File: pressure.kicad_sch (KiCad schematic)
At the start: 14 parts, among them U4 TLV9101IDBVR

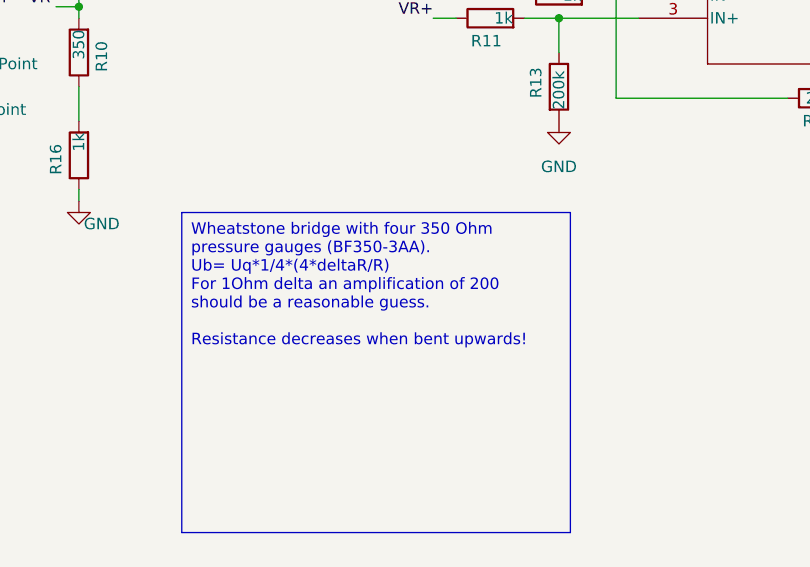
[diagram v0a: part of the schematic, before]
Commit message: update to kicad 9.0 and place Qi-charge IC
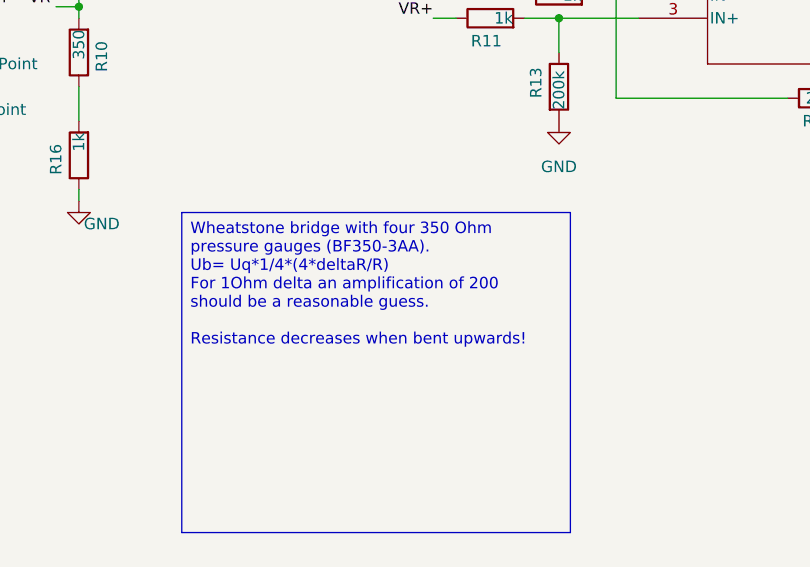
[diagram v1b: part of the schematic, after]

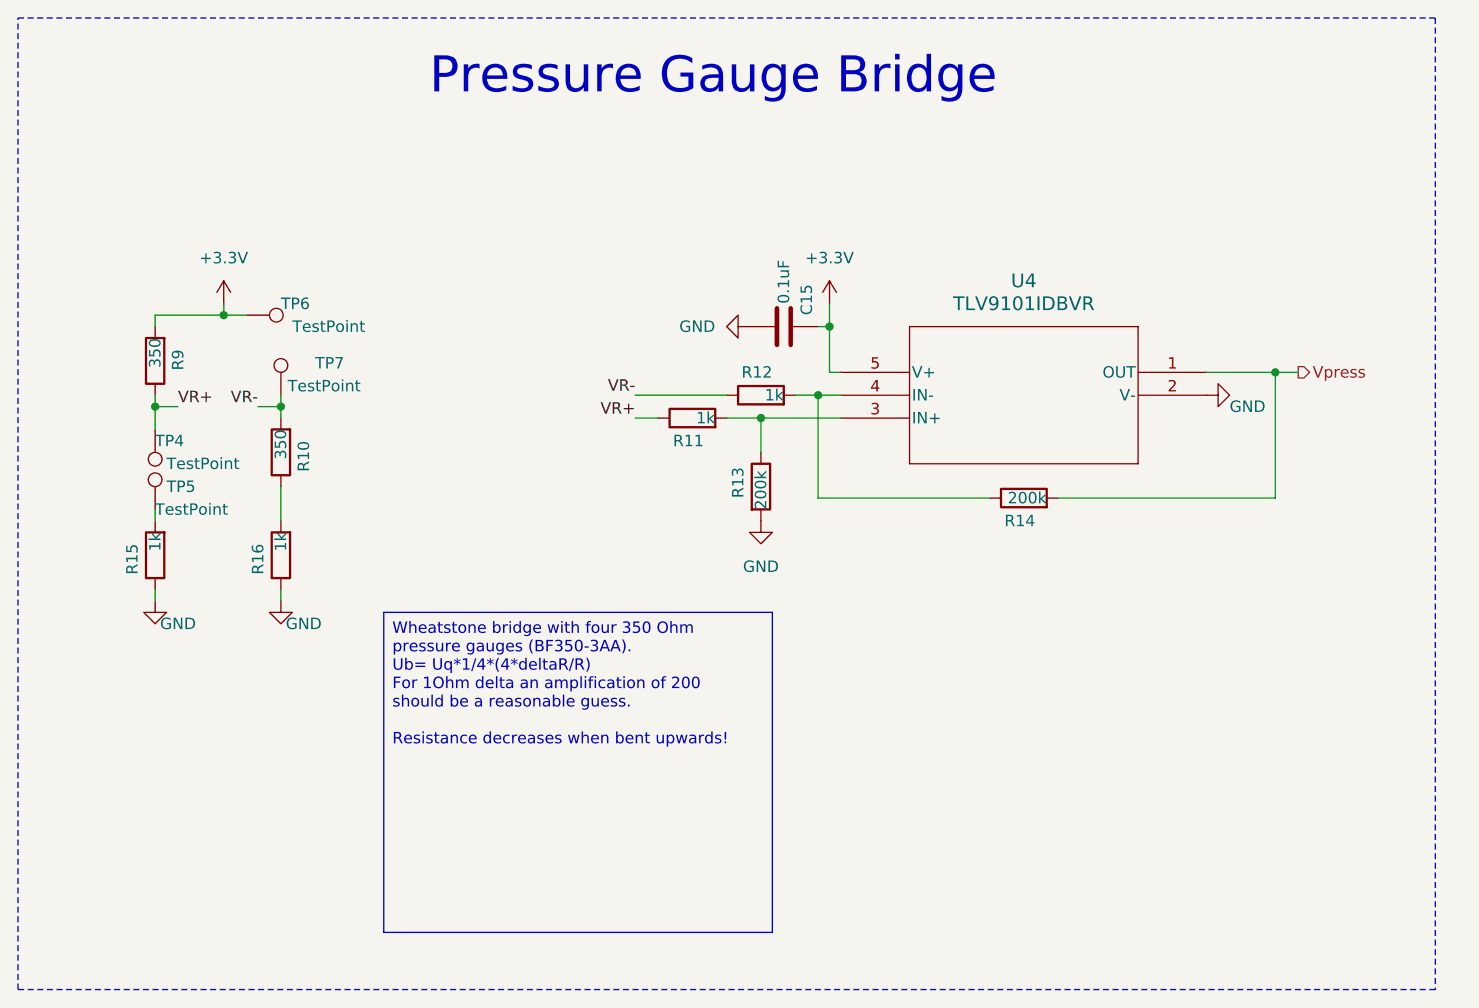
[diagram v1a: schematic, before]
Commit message: implement initial power latching idea
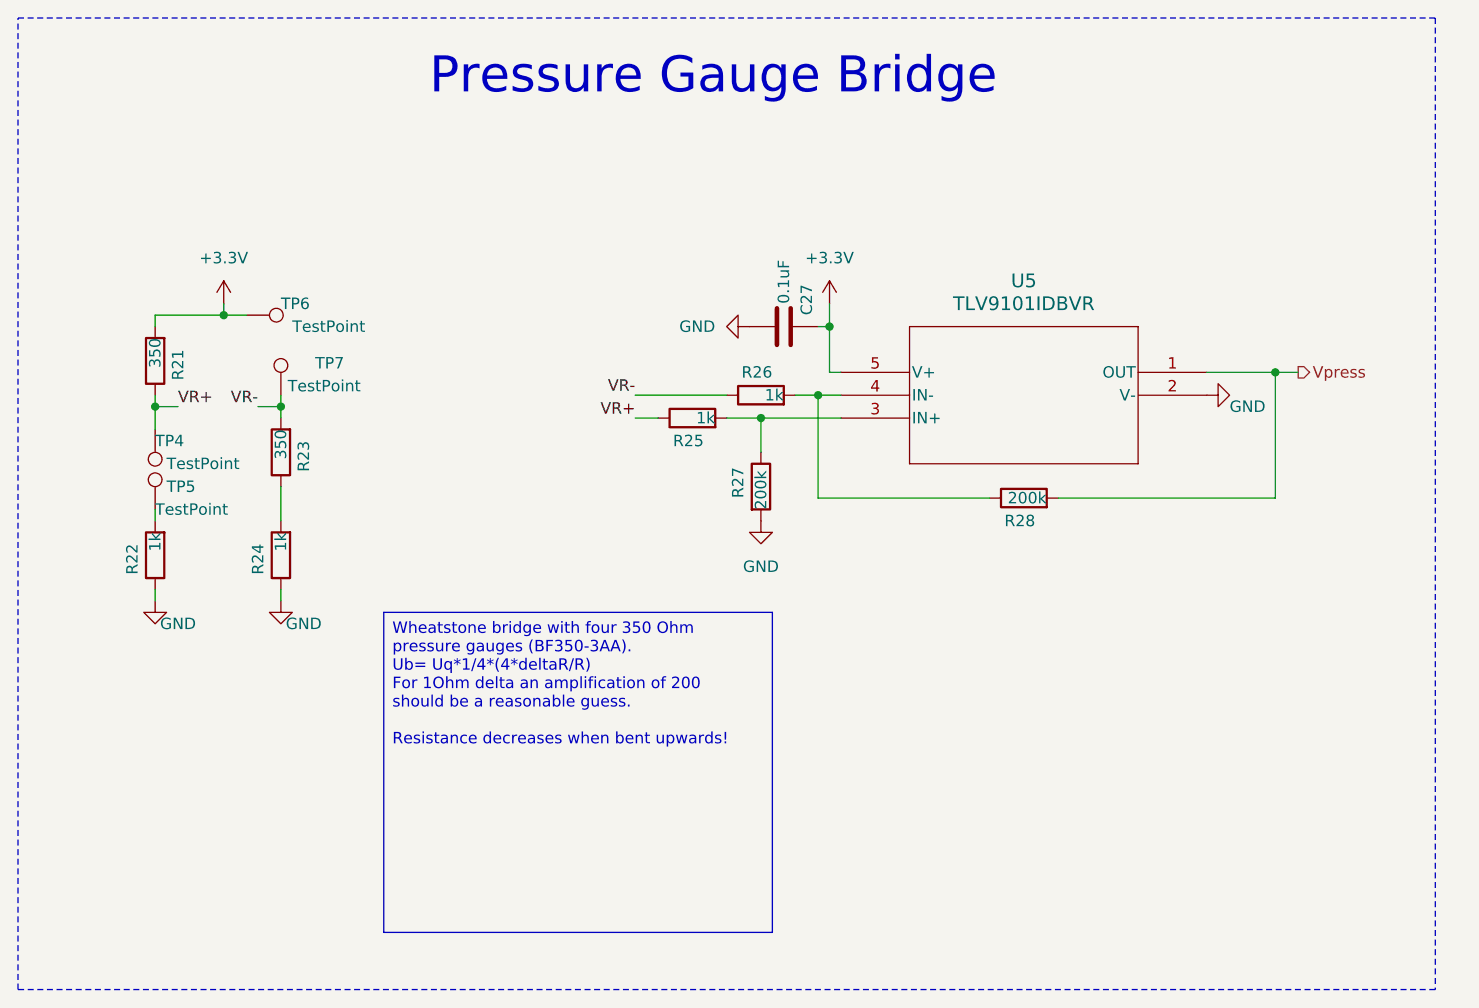
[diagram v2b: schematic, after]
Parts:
- renumbered C15 to C27, R9 to R21, R15 to R22, R10 to R23, R16 to R24, R11 to R25, R12 to R26, R13 to R27, R14 to R28, U4 to U5
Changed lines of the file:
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@@
 		(dnp no)
 		(fields_autoplaced yes)
-		(property "Reference" "#PWR050"
+		(property "Reference" "#PWR067"
 			(at 107.95 82.55 0)
 			(effects
@@
 			(project "bierdeckel"
 				(path "/a4ffe097-37ef-4e19-a91a-ae57f4a5aad1/67cff1c4-a4ae-4e77-90c9-75aa7da1f628"
-					(reference "#PWR050")
+					(reference "#PWR067")
 					(unit 1)
 				)
@@
 		(dnp no)
 		(fields_autoplaced yes)
-		(property "Reference" "#PWR047"
+		(property "Reference" "#PWR064"
 			(at 48.26 55.88 0)
 			(effects
@@
 			(project "bierdeckel"
 				(path "/a4ffe097-37ef-4e19-a91a-ae57f4a5aad1/67cff1c4-a4ae-4e77-90c9-75aa7da1f628"
-					(reference "#PWR047")
+					(reference "#PWR064")
 					(unit 1)
 				)
@@
 		(on_board yes)
 		(dnp no)
-		(property "Reference" "R11"
+		(property "Reference" "R25"
 			(at 101.6 67.31 90)
 			(effects
@@
 			(project "bierdeckel"
 				(path "/a4ffe097-37ef-4e19-a91a-ae57f4a5aad1/67cff1c4-a4ae-4e77-90c9-75aa7da1f628"
-					(reference "R11")
+					(reference "R25")
 					(unit 1)
 				)
@@
 		(on_board yes)
 		(dnp no)
-		(property "Reference" "R9"
+		(property "Reference" "R21"
 			(at 43.18 57.15 90)
 			(effects
@@
 			(project "bierdeckel"
 				(path "/a4ffe097-37ef-4e19-a91a-ae57f4a5aad1/67cff1c4-a4ae-4e77-90c9-75aa7da1f628"
-					(reference "R9")
+					(reference "R21")
 					(unit 1)
 				)
@@
 		(on_board yes)
 		(dnp no)
-		(property "Reference" "R10"
+		(property "Reference" "R23"
 			(at 57.15 67.31 90)
 			(effects
@@
 			(project "bierdeckel"
 				(path "/a4ffe097-37ef-4e19-a91a-ae57f4a5aad1/67cff1c4-a4ae-4e77-90c9-75aa7da1f628"
-					(reference "R10")
+					(reference "R23")
 					(unit 1)
 				)
@@
 		(on_board yes)
 		(dnp no)
-		(property "Reference" "R13"
+		(property "Reference" "R27"
 			(at 105.41 73.66 90)
 			(effects
@@
 			(project "bierdeckel"
 				(path "/a4ffe097-37ef-4e19-a91a-ae57f4a5aad1/67cff1c4-a4ae-4e77-90c9-75aa7da1f628"
-					(reference "R13")
+					(reference "R27")
 					(unit 1)
 				)
@@
 		(on_board yes)
 		(dnp no)
-		(property "Reference" "R12"
+		(property "Reference" "R26"
 			(at 109.22 59.69 90)
 			(effects
@@
 			(project "bierdeckel"
 				(path "/a4ffe097-37ef-4e19-a91a-ae57f4a5aad1/67cff1c4-a4ae-4e77-90c9-75aa7da1f628"
-					(reference "R12")
+					(reference "R26")
 					(unit 1)
 				)
@@
 		(on_board yes)
 		(dnp no)
-		(property "Reference" "#PWR051"
+		(property "Reference" "#PWR068"
 			(at 115.57 55.88 0)
 			(effects
@@
 			(project "bierdeckel"
 				(path "/a4ffe097-37ef-4e19-a91a-ae57f4a5aad1/67cff1c4-a4ae-4e77-90c9-75aa7da1f628"
-					(reference "#PWR051")
+					(reference "#PWR068")
 					(unit 1)
 				)
@@
 		(on_board yes)
 		(dnp no)
-		(property "Reference" "#PWR052"
+		(property "Reference" "#PWR069"
 			(at 163.83 62.23 0)
 			(effects
@@
 			(project "bierdeckel"
 				(path "/a4ffe097-37ef-4e19-a91a-ae57f4a5aad1/67cff1c4-a4ae-4e77-90c9-75aa7da1f628"
-					(reference "#PWR052")
+					(reference "#PWR069")
 					(unit 1)
 				)
@@
 		(on_board yes)
 		(dnp no)
-		(property "Reference" "R16"
+		(property "Reference" "R24"
 			(at 52.07 78.74 90)
 			(effects
@@
 			(project "bierdeckel"
 				(path "/a4ffe097-37ef-4e19-a91a-ae57f4a5aad1/67cff1c4-a4ae-4e77-90c9-75aa7da1f628"
-					(reference "R16")
+					(reference "R24")
 					(unit 1)
 				)
@@
 		(on_board yes)
 		(dnp no)
-		(property "Reference" "C15"
+		(property "Reference" "C27"
 			(at 113.03 53.34 0)
 			(effects
@@
 			(project "bierdeckel"
 				(path "/a4ffe097-37ef-4e19-a91a-ae57f4a5aad1/67cff1c4-a4ae-4e77-90c9-75aa7da1f628"
-					(reference "C15")
+					(reference "C27")
 					(unit 1)
 				)
@@
 		(dnp no)
 		(fields_autoplaced yes)
-		(property "Reference" "#PWR049"
+		(property "Reference" "#PWR066"
 			(at 100.33 54.61 0)
 			(effects
@@
 			(project "bierdeckel"
 				(path "/a4ffe097-37ef-4e19-a91a-ae57f4a5aad1/67cff1c4-a4ae-4e77-90c9-75aa7da1f628"
-					(reference "#PWR049")
+					(reference "#PWR066")
 					(unit 1)
 				)
@@
 		(on_board yes)
 		(dnp no)
-		(property "Reference" "R15"
+		(property "Reference" "R22"
 			(at 38.1 78.74 90)
 			(effects
@@
 			(project "bierdeckel"
 				(path "/a4ffe097-37ef-4e19-a91a-ae57f4a5aad1/67cff1c4-a4ae-4e77-90c9-75aa7da1f628"
-					(reference "R15")
+					(reference "R22")
 					(unit 1)
 				)
@@
 		(on_board yes)
 		(dnp no)
-		(property "Reference" "#PWR046"
+		(property "Reference" "#PWR063"
 			(at 40.64 91.44 0)
 			(effects
@@
 			(project "bierdeckel"
 				(path "/a4ffe097-37ef-4e19-a91a-ae57f4a5aad1/67cff1c4-a4ae-4e77-90c9-75aa7da1f628"
-					(reference "#PWR046")
+					(reference "#PWR063")
 					(unit 1)
 				)
@@
 		(on_board yes)
 		(dnp no)
-		(property "Reference" "#PWR048"
+		(property "Reference" "#PWR065"
 			(at 54.61 91.44 0)
 			(effects
@@
 			(project "bierdeckel"
 				(path "/a4ffe097-37ef-4e19-a91a-ae57f4a5aad1/67cff1c4-a4ae-4e77-90c9-75aa7da1f628"
-					(reference "#PWR048")
+					(reference "#PWR065")
 					(unit 1)
 				)
@@
 		(dnp no)
 		(fields_autoplaced yes)
-		(property "Reference" "U4"
+		(property "Reference" "U5"
 			(at 137.16 49.53 0)
 			(effects
@@
 			(project "bierdeckel"
 				(path "/a4ffe097-37ef-4e19-a91a-ae57f4a5aad1/67cff1c4-a4ae-4e77-90c9-75aa7da1f628"
-					(reference "U4")
+					(reference "U5")
 					(unit 1)
 				)
@@
 		(on_board yes)
 		(dnp no)
-		(property "Reference" "R14"
+		(property "Reference" "R28"
 			(at 138.43 76.2 90)
 			(effects
@@
 			(project "bierdeckel"
 				(path "/a4ffe097-37ef-4e19-a91a-ae57f4a5aad1/67cff1c4-a4ae-4e77-90c9-75aa7da1f628"
-					(reference "R14")
-					(unit 1)
-				)
+					(reference "R28")
+					(unit 1)
+				)

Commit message: before gauge replacement
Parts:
- added IC1: HSFPAR004A, Samacsys:HSFPAR004A, symbol Samacsys:HSFPAR004A
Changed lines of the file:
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@@
+	)
+	(symbol
+		(lib_id "Samacsys:HSFPAR004A")
+		(at 30.48 30.48 0)
+		(unit 1)
+		(exclude_from_sim no)
+		(in_bom yes)
+		(on_board yes)
+		(dnp no)
+		(fields_autoplaced yes)
+		(property "Reference" "IC1"
+			(at 45.72 22.86 0)
+			(effects
+				(font
+					(size 1.27 1.27)
+				)
+			)
+		)
+		(property "Value" "HSFPAR004A"
+			(at 45.72 25.4 0)
+			(effects
+				(font
+					(size 1.27 1.27)
+				)
+			)
+		)
+		(property "Footprint" "Samacsys:HSFPAR004A"
+			(at 57.15 125.4 0)
+			(effects
+				(font
+					(size 1.27 1.27)
+				)
+				(justify left top)
+				(hide yes)
+			)
+		)
+		(property "Datasheet" ""
+			(at 57.15 225.4 0)
+			(effects
+				(font
+					(size 1.27 1.27)
+				)
+				(justify left top)
+				(hide yes)
+			)
+		)
+		(property "Description" "Resistive Force Sensor 0.82kgf (1.8lbs)"
+			(at 30.48 30.48 0)
+			(effects
+				(font
+					(size 1.27 1.27)
+				)
+				(hide yes)
+			)
+		)
+		(property "Height" "0.66"
+			(at 57.15 425.4 0)
+			(effects
+				(font
+					(size 1.27 1.27)
+				)
+				(justify left top)
+				(hide yes)
+			)
+		)
+		(property "Mouser Part Number" "688-HSFPAR004A"
+			(at 57.15 525.4 0)
+			(effects
+				(font
+					(size 1.27 1.27)
+				)
+				(justify left top)
+				(hide yes)
+			)
+		)
+		(property "Mouser Price/Stock" "https://www.mouser.co.uk/ProductDetail/Alps-Alpine/HSFPAR004A?qs=XeJtXLiO41SKORml6bvmQg%3D%3D"
+			(at 57.15 625.4 0)
+			(effects
+				(font
+					(size 1.27 1.27)
+				)
+				(justify left top)
+				(hide yes)
+			)
+		)
+		(property "Manufacturer_Name" "ALPS Electric"
+			(at 57.15 725.4 0)
+			(effects
+				(font
+					(size 1.27 1.27)
+				)
+				(justify left top)
+				(hide yes)
+			)
+		)
+		(property "Manufacturer_Part_Number" "HSFPAR004A"
+			(at 57.15 825.4 0)
+			(effects
+				(font
+					(size 1.27 1.27)
+				)
+				(justify left top)
+				(hide yes)
+			)
+		)
+		(pin "4"
+		)
+		(pin "3"
+		)
+		(pin "2"
+		)
+		(pin "1"
+		)
+		(pin "5"
+		)
+		(instances
+			(project ""
+				(path "/a4ffe097-37ef-4e19-a91a-ae57f4a5aad1/67cff1c4-a4ae-4e77-90c9-75aa7da1f628"
+					(reference "IC1")
+					(unit 1)
+				)
+			)
+		)
 	)
 	(symbol
